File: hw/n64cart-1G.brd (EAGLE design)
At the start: 99.1 x 50.8 mm, 37 parts, among them IC1 RP2040-QFN56, J1 N64_EDGE, Q1 BSS84, U4 MX66L1G45GMI-08GSOP_16L_300_M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

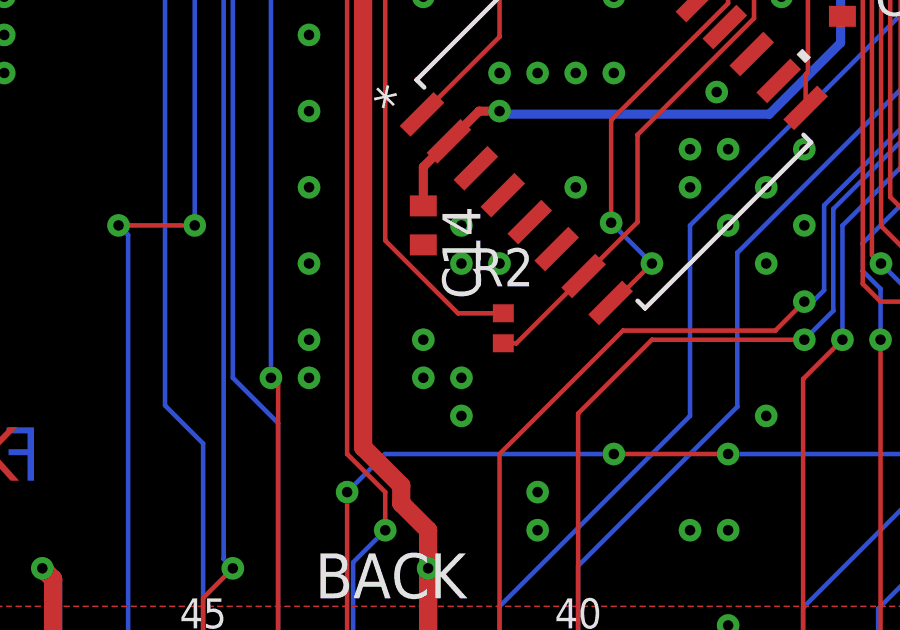
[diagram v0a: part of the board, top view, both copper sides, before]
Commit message: 1Gbit pdf schematic
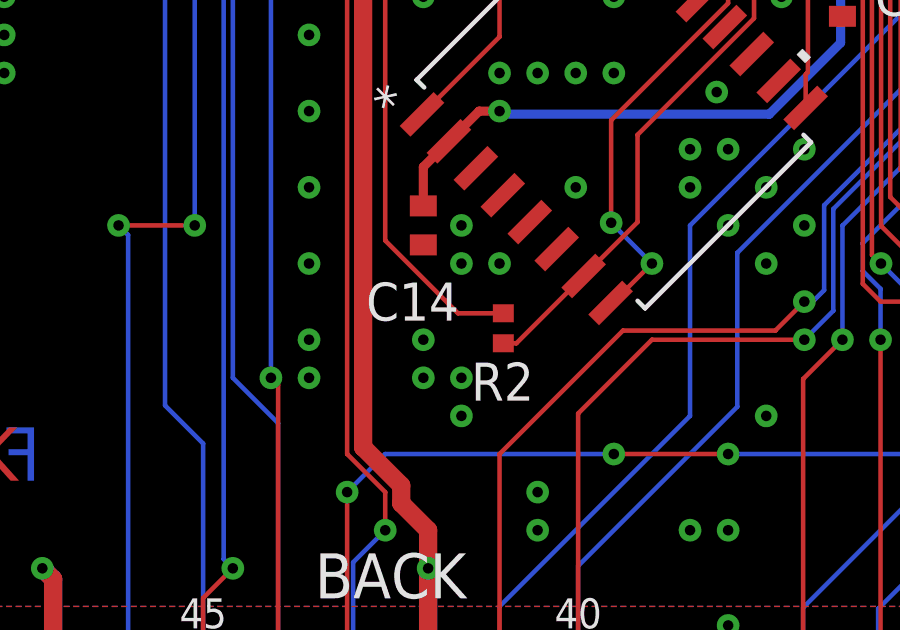
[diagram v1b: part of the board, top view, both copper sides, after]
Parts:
- D1: value SL02-GS08DIODE_SL02-GS08_VIS-M -> SL02-GS08
- D3: value GREEN -> RED
- U4: value MX66L1G45GMI-08GSOP_16L_300_MAC-L -> MX66L1G45GMI-08G
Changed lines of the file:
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@@
 </element>
 <element name="C14" library="rcl" library_urn="urn:adsk.eagle:library:334" package="C0402" package3d_urn="urn:adsk.eagle:package:23626/2" value="100n" x="39.37" y="22.86" smashed="yes" rot="R270">
-<attribute name="NAME" x="40.005" y="23.495" size="1.27" layer="25" rot="R270"/>
+<attribute name="NAME" x="37.465" y="19.685" size="1.27" layer="25"/>
 <attribute name="POPULARITY" value="18" x="39.37" y="22.86" size="1.778" layer="27" rot="R270" display="off"/>
 <attribute name="SPICEPREFIX" value="C" x="39.37" y="22.86" size="1.778" layer="27" rot="R270" display="off"/>
@@
 </element>
 <element name="R2" library="rcl" library_urn="urn:adsk.eagle:library:334" package="R0402" package3d_urn="urn:adsk.eagle:package:23547/3" value="1K" x="42.037" y="19.431" smashed="yes" rot="R90">
-<attribute name="NAME" x="43.053" y="22.098" size="1.27" layer="25" rot="R180"/>
+<attribute name="NAME" x="43.053" y="18.288" size="1.27" layer="25" rot="R180"/>
 <attribute name="POPULARITY" value="0" x="42.037" y="19.431" size="1.778" layer="27" rot="R90" display="off"/>
 <attribute name="SPICEPREFIX" value="R" x="42.037" y="19.431" size="1.778" layer="27" rot="R90" display="off"/>
@@
 <attribute name="VALUE" x="23.495" y="51.435" size="1.27" layer="27" rot="R90"/>
 </element>
-<element name="U4" library="MX66L1G45GMI-08G" package="SOP_16L_300_MAC-L" value="MX66L1G45GMI-08GSOP_16L_300_MAC-L" x="45.72" y="26.67" smashed="yes" rot="R45">
+<element name="U4" library="MX66L1G45GMI-08G" package="SOP_16L_300_MAC-L" value="MX66L1G45GMI-08G" x="45.72" y="26.67" smashed="yes" rot="R45">
 <attribute name="COPYRIGHT" value="Copyright (C) 2024 Ultra Librarian. All rights reserved." x="45.72" y="26.67" size="1.778" layer="27" rot="R45" display="off"/>
 <attribute name="MANUFACTURER_PART_NUMBER" value="MX66L1G45GMI-08G" x="45.72" y="26.67" size="1.778" layer="27" rot="R45" display="off"/>
@@
 <attribute name="VALUE" x="65.405" y="48.895" size="1.27" layer="28" rot="MR0"/>
 </element>
-<element name="D3" library="microbuilder" package="CHIPLED_0603_NOOUTLINE" value="GREEN" x="81.28" y="50.8" smashed="yes" rot="MR90">
+<element name="D3" library="microbuilder" package="CHIPLED_0603_NOOUTLINE" value="RED" x="81.28" y="50.8" smashed="yes" rot="MR90">
 <attribute name="NAME" x="80.645" y="52.324" size="0.8128" layer="26" ratio="18" rot="MR180"/>
 <attribute name="VALUE" x="80.01" y="52.07" size="0.4064" layer="28" ratio="10" rot="MR180"/>
 </element>
-<element name="D1" library="SL02-GS08" package="DIODE_SL02-GS08_VIS-M" value="SL02-GS08DIODE_SL02-GS08_VIS-M" x="10.16" y="49.53" smashed="yes" rot="R180">
+<element name="D1" library="SL02-GS08" package="DIODE_SL02-GS08_VIS-M" value="SL02-GS08" x="10.16" y="49.53" smashed="yes" rot="R180">
 <attribute name="COPYRIGHT" value="Copyright (C) 2022 Ultra Librarian. All rights reserved." x="10.16" y="49.53" size="1.778" layer="27" rot="R180" display="off"/>
 <attribute name="DIGI-KEY_PART_NUMBER_1" value="SL02-GS08TR-ND" x="10.16" y="49.53" size="1.778" layer="27" rot="R180" display="off"/>
